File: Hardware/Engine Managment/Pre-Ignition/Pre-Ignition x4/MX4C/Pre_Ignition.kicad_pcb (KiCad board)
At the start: 2 copper layers, 100 x 100 mm, 152 parts, among them IC1 L78M05ABDT-TR, J1 Conn_02x12_Counter_Clockwise, J2 Serial0, J3 Serial3, J4 Map/Baro Sensor Socket, J5 Conn_02x12_Counter_Clockwise, J6 VR_Header, J7 Conn_02x10_Counter_Clockwise, Q1 IRFR024, Q10 AO3400A, Q11 AO3400A, Q2 IRFR024, Q3 IRFR024, Q4 IRFR024, Q5 AO3400A, Q6 AO3400A, Q7 AO3400A, Q8 AO3400A, Q9 AO3400A, U1 SRV05-4-P-T7, U2 TC4424, U3 TC4424, U4 SRV05-4-P-T7, U5 SRV05-4-P-T7, U6 ULN2003A

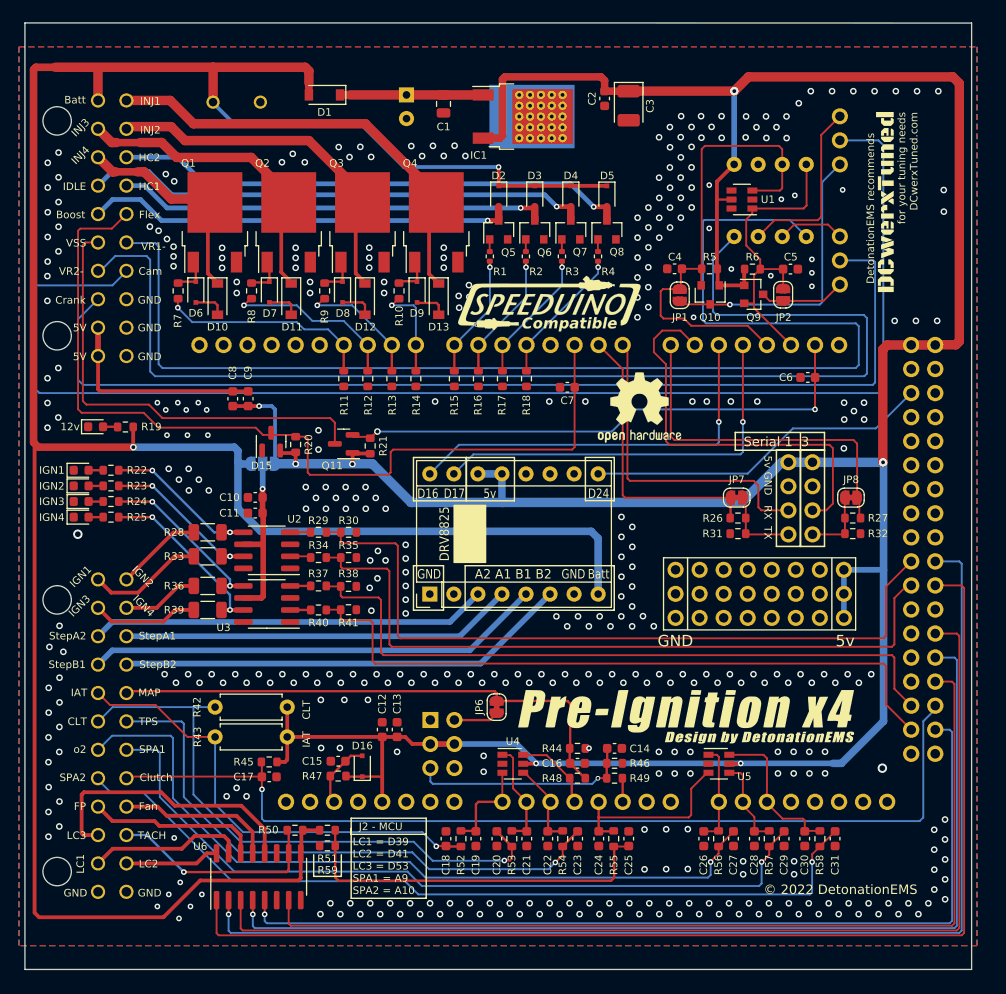
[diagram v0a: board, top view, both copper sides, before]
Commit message: Upload correct initial upload files
Initial upload files were accidently taken from an alpha folder. 5v pins on main connector had no voltage. To fix the issue on any manufactured boards remove C8 and C9. Then short the pins of the removed capacitors.
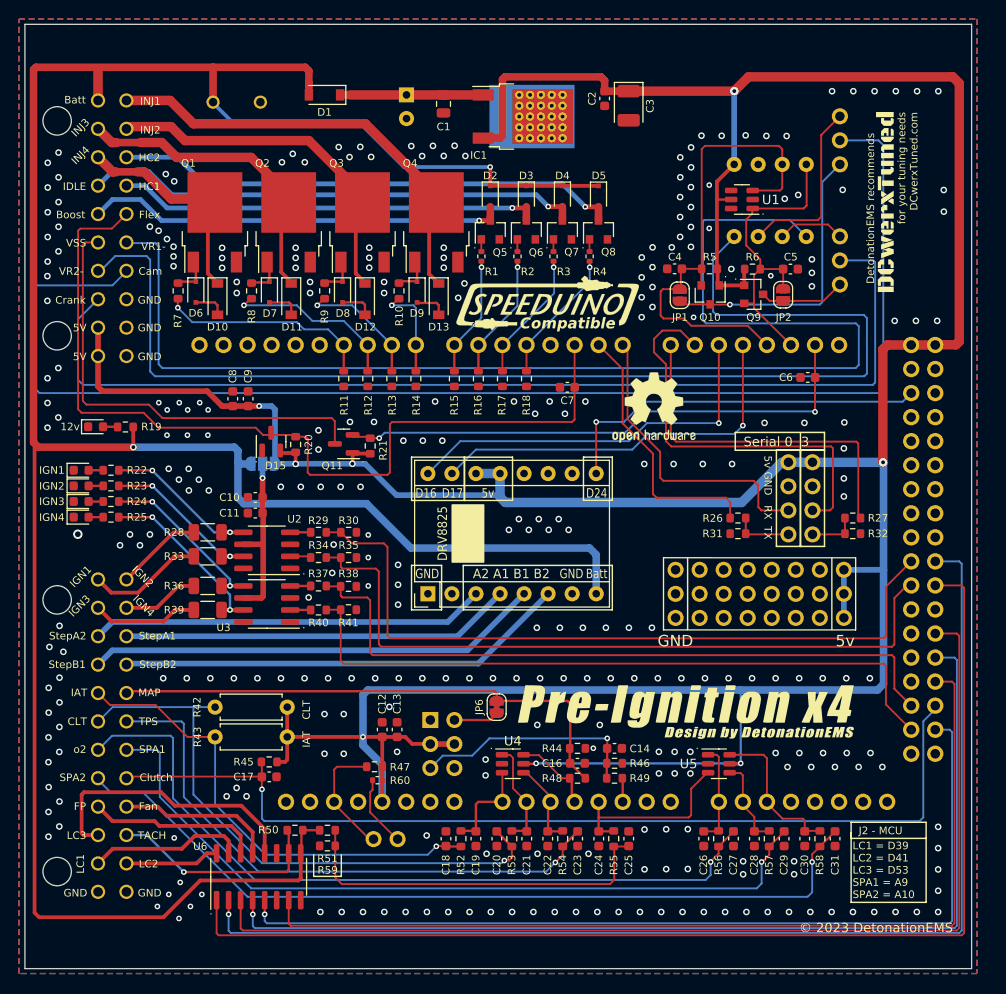
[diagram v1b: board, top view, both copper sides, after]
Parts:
- removed C15: 4.7nF, Capacitor_SMD:C_0603_1608Metric
- removed D16: 1N4148WS, Diode_SMD:D_SOD-323F
- removed G2: OSHW, Symbol:OSHW-Logo2_9.8x8mm_SilkScreen
- removed JP7, JP8: SolderJumper_2_Bridged, Jumper:SolderJumper-2_P1.3mm_Bridged_RoundedPad1.0x1.5mm
- added J8: Reset Control, Detonation:1x02-Proto, B.Cu at (120.8, 136.0)
- added R60: 120, Resistor_SMD:R_0402_1005Metric, F.Cu at (121.2, 129.8)
- added REF**: OSHW-Logo2_9.8x8mm_SilkScreen, Symbol:OSHW-Logo2_9.8x8mm_SilkScreen, F.Cu at (150.4, 90.4)
- moved R47 3.97 mm to (120.9, 128.4)
- moved D5 0.89 mm to (144.5, 68.1)
- moved Q8 0.89 mm to (144.5, 71.7)
- moved R1 0.89 mm to (132.1, 74.5)
- moved R2 0.89 mm to (136.0, 74.5)
- moved R3 0.89 mm to (139.8, 74.5)
- moved R4 0.89 mm to (143.6, 74.5)
- moved D2 0.89 mm to (133.1, 68.1)
- moved D3 0.89 mm to (136.9, 68.1)
- moved D4 0.89 mm to (140.7, 68.1)
- moved Q5 0.89 mm to (133.1, 71.7)
- moved Q6 0.89 mm to (136.9, 71.7)
- moved Q7 0.89 mm to (140.7, 71.7)
- moved G4 0.51 mm to (153.7, 122.0)
- moved G5 0.51 mm to (161.5, 124.8)
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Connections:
- net IGN-V renamed Net-(JP3-C)
- C8 pad 2: VDDA -> GND
- C9 pad 2: VDDA -> GND
- J7 pad 10: VDDA -> VDD
- J7 pad 9: VDDA -> VDD
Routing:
- net VDD: track 345.1 -> 407.0 mm, vias 7 -> 8
- net VDDA: track 22.4 -> 0.00 mm
- net Net-(J8-Pin_2): track 0.00 -> 7.17 mm
- net MC-RESET: track 6.92 -> 11.9 mm
- net MC-D24: track 36.6 -> 40.0 mm, vias 0 -> 1
- net +BATT: track 291.3 -> 288.5 mm
- net MC-D1-TX: track 30.5 -> 28.3 mm
- net Net-(J3-Pin_4): track 7.15 -> 5.00 mm
- net MC-D0-RX: track 33.3 -> 31.3 mm
- net Net-(J2-Pin_4): track 8.07 -> 6.21 mm
- net MC-D17: track 42.8 -> 41.3 mm
- net MC-D16: track 42.2 -> 41.2 mm
- net BOOST: track 45.3 -> 44.4 mm
- net IDLE: track 53.5 -> 52.7 mm
- net HC2: track 54.4 -> 53.5 mm
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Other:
- board size 100 x 100 mm -> 100 x 99.8 mm
- board text added: "."
- board text added: "JP1-BRIDGE TO DISABLE CAM INPUT BUFFER JP2-BRIDGE TO DISABLE CRANK INPUT BUFFER JP6-SEVER FOR EXTERNAL MAP SENSOR"
- board text added: "JP3-Ignition Voltage Output: 150ma MAX For use with Igniter (ICM) or 'Smart' Coil ONLY! 1-2 - 5v (Default) 2-3 - Batt (MUST SEVER 1-2)"
- board text added: "Serial 0 3"
- board text added: "© 2023 DetonationEMS"
- board text removed: "J4 - For use with (PN# PMAP-L) Open jumper JP6 to use external map sensor pin on connector J5"
- board text removed: "JP3 - Ignition Voltage Output: 150ma MAX For use with Igniter (ICM) or 'Smart' Coil ONLY! 1-2 - 5v (Default) 2-3 - Batt (MUST OPEN 1-2)"
- board text removed: "Serial 1 3"
- board text removed: "© 2022 DetonationEMS"

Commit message: Structure Update
MX2 - RevB Upload
MX4B-2 - KiCad Version update (no changes)
MX4C - Organized Schematic, Minor layout change
Engine Simulator 8 Channel - Organized Schematic (no changes)
PMAP-M - Map Sensor Breakout for MX4C
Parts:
- removed the C3 at (147.7, 58.5)
- removed C32: 10uF, Capacitor_THT:CP_Radial_Tantal_D5.0mm_P2.50mm
- removed the C8 at (105.9, 89.5)
- removed the C9 at (107.5, 89.5)
- removed the G3 at (139.1, 79.4)
- added C2: 2.2uF, Capacitor_SMD:C_1206_3216Metric, F.Cu at (131.7, 58.8)
- added C4: 10uF, Capacitor_Tantalum_SMD:CP_EIA-3216-18_Kemet-A, F.Cu at (140.8, 65.6)
- added D2: ZMM5V6-M, Diode_SMD:D_MiniMELF, F.Cu at (143.3, 66.0)
- added G25: LOGO, Detonation-Logos:SpeeduinoCompatible-17mm, F.Cu at (158.8, 58.5)
- A1: footprint Module:Pololu_Breakout-16_15.2x20.3mm -> Detonation:DVR8825-Labeled-Front
- D1: value B5819W -> SS34; footprint Diode_SMD:D_SOD-123 -> Diode_SMD:D_SMA
- IC1: footprint Detonation:TO-252-2-Thermal-Pad -> Detonation:TO-252-2-Thermal
- R10: renamed from R4; value 120 -> 470r
- R7: renamed from R1; value 120 -> 470r
- R8: renamed from R2; value 120 -> 470r
- R9: renamed from R3; value 120 -> 470r
- moved C3 9.52 mm to (138.8, 64.9)
- moved D1 8.30 mm to (123.9, 57.8)
- moved C1 6.02 mm to (134.2, 58.3)
- moved IC1 5.24 mm to (141.8, 59.6)
- moved D6 4.91 mm to (146.0, 72.8)
- moved Q8 4.91 mm to (146.0, 76.4)
- moved R10 4.91 mm to (145.0, 79.1)
- moved R9 4.86 mm to (141.0, 79.1)
- moved D5 4.86 mm to (142.0, 72.8)
- moved Q7 4.86 mm to (142.0, 76.4)
- moved R8 4.80 mm to (137.0, 79.1)
- moved D4 4.80 mm to (138.0, 72.8)
- moved Q6 4.80 mm to (138.0, 76.3)
- moved R7 4.77 mm to (133.1, 79.1)
- moved D3 4.77 mm to (134.0, 72.8)
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- renumbered C11 to C10, C12 to C11, C13 to C12, C14 to C13, C16 to C14, C17 to C15, C18 to C16, C19 to C17, C20 to C18, C21 to C19, C22 to C20, C23 to C21, C24 to C22, C25 to C23, C26 to C24, C27 to C25, C28 to C26, C29 to C27, C30 to C28, C31 to C29, C2 to C3, C4 to C5, C5 to C6, C6 to C7, C7 to C8, C10 to C9, D9 to D10, D10 to D11, D11 to D12, D12 to D13, D13 to D14, D14 to D15, D15 to D16, D2 to D3, D3 to D4, D4 to D5, D5 to D6, D6 to D7, D7 to D8, D8 to D9, G4 to G2, G5 to G3, REF** to G99, J2 to J1, J3 to J2, J1 to J3, J7 to J4, J6 to J5, J5 to J6, J4 to J7, JP2 to JP1, JP1 to JP2, JP6 to JP3, JP5 to JP4, JP4 to JP5, JP3 to JP6, Q9 to Q10, Q10 to Q9, R5 to R1, R6 to R2, R7 to R3, R8 to R4, R9 to R5, R60 to R50, R50 to R51, R51 to R52, R52 to R53, R53 to R54, R54 to R55, R55 to R56, R56 to R57, R57 to R58, R58 to R59, R10 to R6, R59 to R60
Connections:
- net 12v-Protected renamed +Batt-Protected
- net Net-(JP3-C) renamed IGN-PWR
- net VDD renamed +5V
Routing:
- net +BATT: track 288.5 -> 281.8 mm, vias 2 -> 1
- net +5V: track 407.0 -> 400.8 mm
- net +Batt-Protected: track 15.1 -> 10.3 mm
- net MC-D7: track 12.8 -> 8.12 mm
- net MC-D6: track 13.3 -> 9.65 mm
- net HC2: track 53.5 -> 56.9 mm
- net IDLE: track 52.7 -> 55.9 mm
- net HC1: track 44.7 -> 47.8 mm
- net BOOST: track 44.4 -> 47.3 mm
- net MC-D5: track 13.8 -> 11.1 mm
- net MC-D4: track 14.2 -> 12.6 mm
- net Crank-In: track 110.4 -> 109.1 mm
- net Net-(JP2-A): track 30.1 -> 28.9 mm
- net Net-(JP1-A): track 9.11 -> 7.91 mm
- net Cam-VR: track 19.0 -> 17.8 mm
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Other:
- board text added: "1"
- board text added: "3"
- board text added: "A2"
- board text added: "B1"
- board text added: "JP1-BRIDGE TO DISABLE CRANK INPUT BUFFER JP2-BRIDGE TO DISABLE CAM INPUT BUFFER JP3-SEVER FOR EXTERNAL MAP SENSOR"
- board text added: "JP6-Ignition Voltage Output: 150ma MAX For use with Igniter (ICM) or 'Smart' Coil ONLY! 1-2 - 5v (Default) 2-3 - Batt (MUST SEVER 1-2)"
- board text added: "locked"
- board text removed: "A2 A1 B1 B2"
- board text removed: "Clutch"
- board text removed: "D16"
- board text removed: "D17"
- board text removed: "D24"
- board text removed: "DRV8825"
- board text removed: "Fan"
- board text removed: "IGN1"
- board text removed: "IGN2"
- board text removed: "IGN3"
- board text removed: "IGN4"
- board text removed: "JP1-BRIDGE TO DISABLE CAM INPUT BUFFER JP2-BRIDGE TO DISABLE CRANK INPUT BUFFER JP6-SEVER FOR EXTERNAL MAP SENSOR"
- board text removed: "JP3-Ignition Voltage Output: 150ma MAX For use with Igniter (ICM) or 'Smart' Coil ONLY! 1-2 - 5v (Default) 2-3 - Batt (MUST SEVER 1-2)"
- board text removed: "LC2"
- board text removed: "MAP"
- board text removed: "SPA1"
- board text removed: "StepA1"
- board text removed: "StepA2"
- board text removed: "StepB1"
- board text removed: "StepB2"
- board text removed: "TACH"
- board text removed: "TPS"

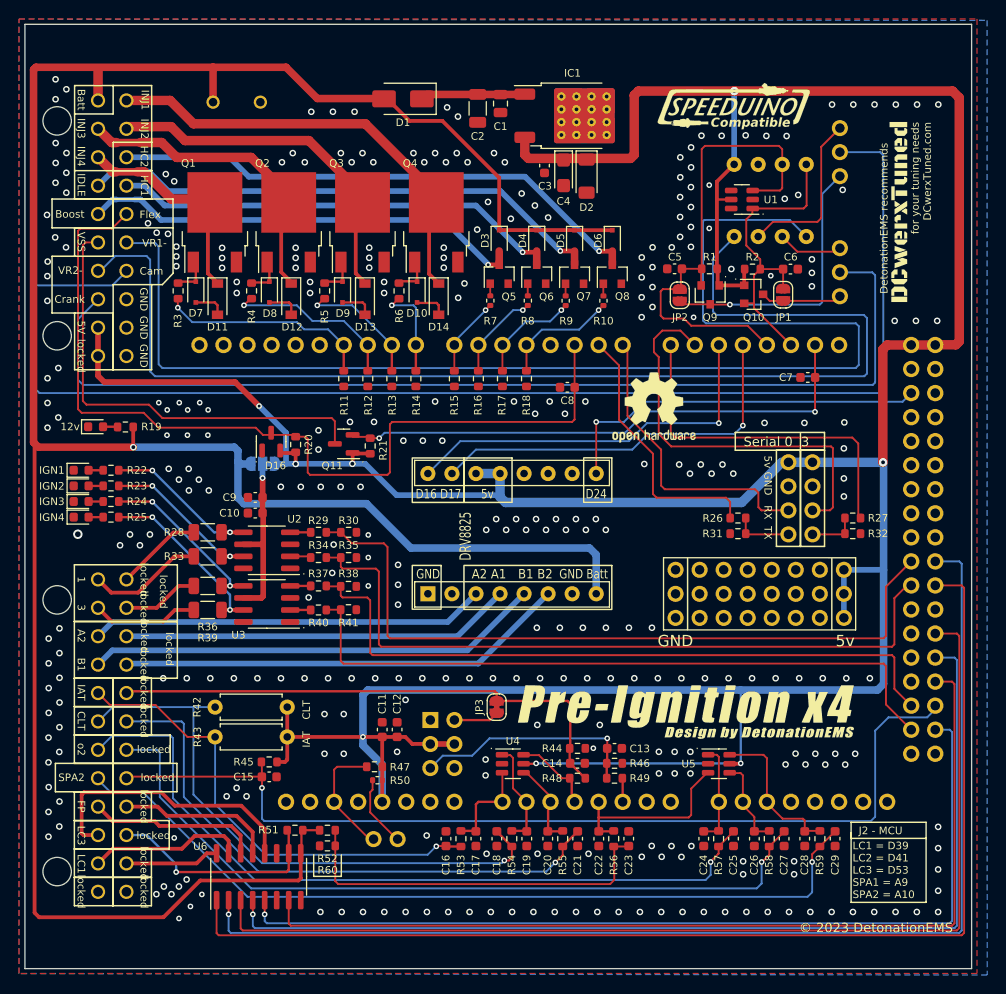
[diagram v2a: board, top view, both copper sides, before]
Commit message: minor update
Copper Pour and clearances updated.
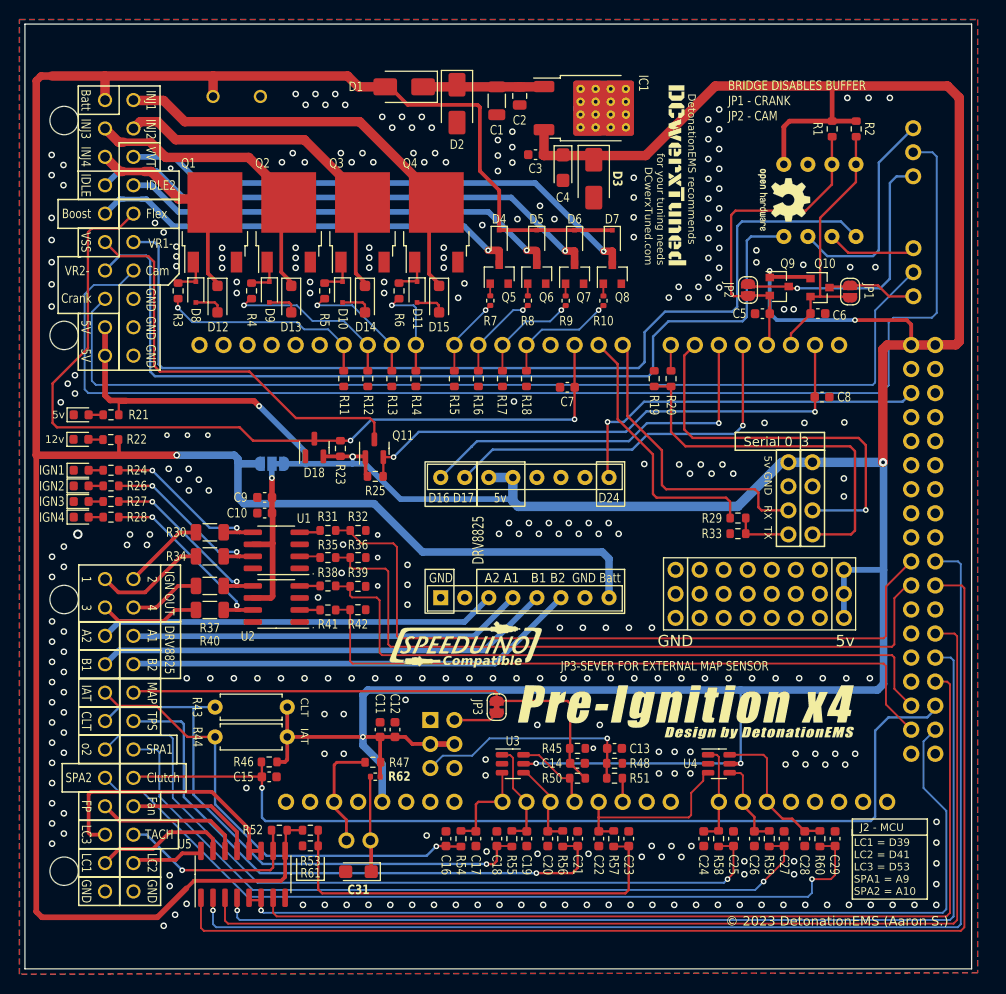
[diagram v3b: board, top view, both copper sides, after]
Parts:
- removed the D14 at (127.6, 79.0)
- removed the R50 at (121.2, 129.8)
- removed the U1 at (159.7, 68.5)
- added C31: 10uF, Capacitor_Tantalum_SMD:CP_EIA-3216-18_Kemet-A, F.Cu at (119.2, 139.5)
- added D15: SMF30CA, Diode_SMD:D_SOD-123F, F.Cu at (127.7, 79.0)
- added D16: LED-Green, LED_SMD:LED_0603_1608Metric, F.Cu at (89.9, 91.2)
- added D3: TVS 5.0A, Diode_SMD:D_SMA, F.Cu at (144.0, 66.3)
- added R21: 1k, Resistor_SMD:R_0603_1608Metric, F.Cu at (93.0, 91.2)
- added R62: 470r, Resistor_SMD:R_0402_1005Metric, F.Cu at (120.9, 129.4)
- D1: value SS34 -> M7
- D12: renamed from D11; value DDZ36-7 -> SMF30CA; footprint Diode_SMD:D_SOD-123 -> Diode_SMD:D_SOD-123F
- D13: renamed from D12; value DDZ36-7 -> SMF30CA; footprint Diode_SMD:D_SOD-123 -> Diode_SMD:D_SOD-123F
- D14: renamed from D13; value DDZ36-7 -> SMF30CA; footprint Diode_SMD:D_SOD-123 -> Diode_SMD:D_SOD-123F
- D2: value ZMM5V6-M -> TVS 26a; footprint Diode_SMD:D_MiniMELF -> Diode_SMD:D_SMA
- G2: renamed from G99; value OSHW-Logo2_9.8x8mm_SilkScreen -> OSHW-Logo2_7.3x6mm_SilkScreen; footprint Symbol:OSHW-Logo2_9.8x8mm_SilkScreen -> Symbol:OSHW-Logo2_7.3x6mm_SilkScreen
- J5: footprint Detonation:Socket_VRConditioner -> Detonation:Socket_VRConditioner_Corrected
- JP3: value SolderJumper_2_Bridged -> MAP bypass
- JP4, JP5: footprint Detonation:1x03_Horizontal_2.54mm -> Detonation:1x03-Proto
- moved G3 63.5 mm to (130.5, 115.4)
- moved R19 26.6 mm to (150.4, 87.4), turned to -90 degrees
- moved G2 25.9 mm to (164.1, 68.5), turned to -90 degrees
- moved R20 24.2 mm to (152.2, 87.4), turned to 90 degrees
- moved G1 23.7 mm to (152.8, 65.9), turned to -90 degrees
- moved R1 19.7 mm to (169.2, 61.0), turned to -90 degrees
- moved R2 18.4 mm to (171.7, 61.0), turned to -90 degrees
- moved D2 15.7 mm to (129.6, 58.3)
- moved C5 10.4 mm to (161.8, 80.5)
- moved JP5 7.77 mm to (177.8, 78.7)
- moved JP4 7.74 mm to (177.8, 66.0)
- moved Q9 7.35 mm to (163.6, 77.6), turned to 0 degrees
- moved JP2 7.23 mm to (160.3, 78.0), turned to -90 degrees
- moved JP1 7.08 mm to (171.1, 78.2), turned to -90 degrees
- moved Q10 7.04 mm to (167.9, 77.8)
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- renumbered C2 to C1, C1 to C2, C8 to C7, C7 to C8, D9 to D10, D10 to D11, D15 to D17, D16 to D18, D3 to D4, D4 to D5, D5 to D6, D6 to D7, D7 to D8, D8 to D9, G25 to G3, G2 to G4, G3 to G5, R32 to R19, R27 to R20, R19 to R22, R20 to R23, R22 to R24, R21 to R25, R23 to R26, R24 to R27, R25 to R28, R26 to R29, R28 to R30, R29 to R31, R30 to R32, R31 to R33, R33 to R34, R34 to R35, R35 to R36, R36 to R37, R37 to R38, R38 to R39, R39 to R40, R40 to R41, R41 to R42, R42 to R43, R43 to R44, R44 to R45, R45 to R46, R46 to R48, R48 to R50, R49 to R51, R51 to R52, R52 to R53, R53 to R54, R54 to R55, R55 to R56, R56 to R57, R57 to R58, R58 to R59, R59 to R60, R60 to R61, U2 to U1, U3 to U2, U4 to U3, U5 to U4, U6 to U5
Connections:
- net HC1 renamed IDLE2
- net HC2 renamed VVT
- C1 pad 1: +Batt-Protected -> Net-(D1-K)
- C2 pad 1: +Batt-Protected -> Net-(D1-K)
- D1 pad 1: +Batt-Protected -> Net-(D1-K)
- D2 pad 1: +5V -> Net-(D1-K)
- IC1 pad 1: +Batt-Protected -> Net-(D1-K)
- U5 pad 11: unconnected-(U6-O6-Pad11) -> D53
- U5 pad 6: unconnected-(U6-I6-Pad6) -> MC-D53
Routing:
- net Net-(J2-Pin_4): track 5.00 -> 39.9 mm
- net MC-D14-TX: track 37.2 -> 2.70 mm
- net VR1-: track 133.2 -> 103.0 mm
- net VR2-: track 125.1 -> 97.6 mm
- net MC-D18: track 51.6 -> 35.3 mm
- net +5V: track 400.8 -> 412.9 mm
- net Net-(D1-K): track 0.00 -> 11.7 mm
- net +Batt-Protected: track 10.3 -> 0.00 mm
- net Cam-In: track 140.8 -> 133.0 mm
- net +BATT: track 281.8 -> 276.0 mm
- net Net-(C23-Pad1): track 40.2 -> 45.5 mm
- net Cam-VR: track 17.8 -> 23.0 mm
- net MC-D19: track 32.4 -> 28.4 mm
- net VSS: track 48.2 -> 44.6 mm
- net Crank-In: track 109.1 -> 105.6 mm
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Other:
- board text added: "2"
- board text added: "4"
- board text added: "A1"
- board text added: "Auxiliary Inputs and Outputs LC 1-2 - Ground Switching Out (300ma MAX) LC 3 - Ground Switching Out (600ma MAX) SPA - Spare Analog Input (0-5v)"
- board text added: "B2"
- board text added: "BRIDGE DISABLES BUFFER JP1 - CRANK JP2 - CAM"
- board text added: "Clutch"
- board text added: "DRV8825"
- board text added: "Fan"
- board text added: "IDLE2"
- board text added: "IGN OUT"
- board text added: "JP3-SEVER FOR EXTERNAL MAP SENSOR"
- board text added: "LC2"
- board text added: "MAP"
- board text added: "SPA1"
- board text added: "TACH"
- board text added: "TPS"
- board text added: "VVT"
- board text added: "© 2023 DetonationEMS (Aaron S.)"
- board text removed: "Auxiliary Inputs and Outputs LC - Ground Switching Out (300ma MAX) SPA - Spare Analog Input (0-5v)"
- board text removed: "HC1"
- board text removed: "HC2"
- board text removed: "JP1-BRIDGE TO DISABLE CRANK INPUT BUFFER JP2-BRIDGE TO DISABLE CAM INPUT BUFFER JP3-SEVER FOR EXTERNAL MAP SENSOR"
- board text removed: "locked"
- board text removed: "© 2023 DetonationEMS"
